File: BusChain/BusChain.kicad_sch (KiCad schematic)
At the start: 32 parts, among them J1 Bonn_01x07, J10 Bonn_01x04, J11 Bonn_01x04, J12 Bonn_01x04, J13 Bonn_01x04, J14 Bonn_01x04, J15 Bonn_01x04, J16 Bonn_01x04, J17 Bonn_01x04, J18 Bonn_01x07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

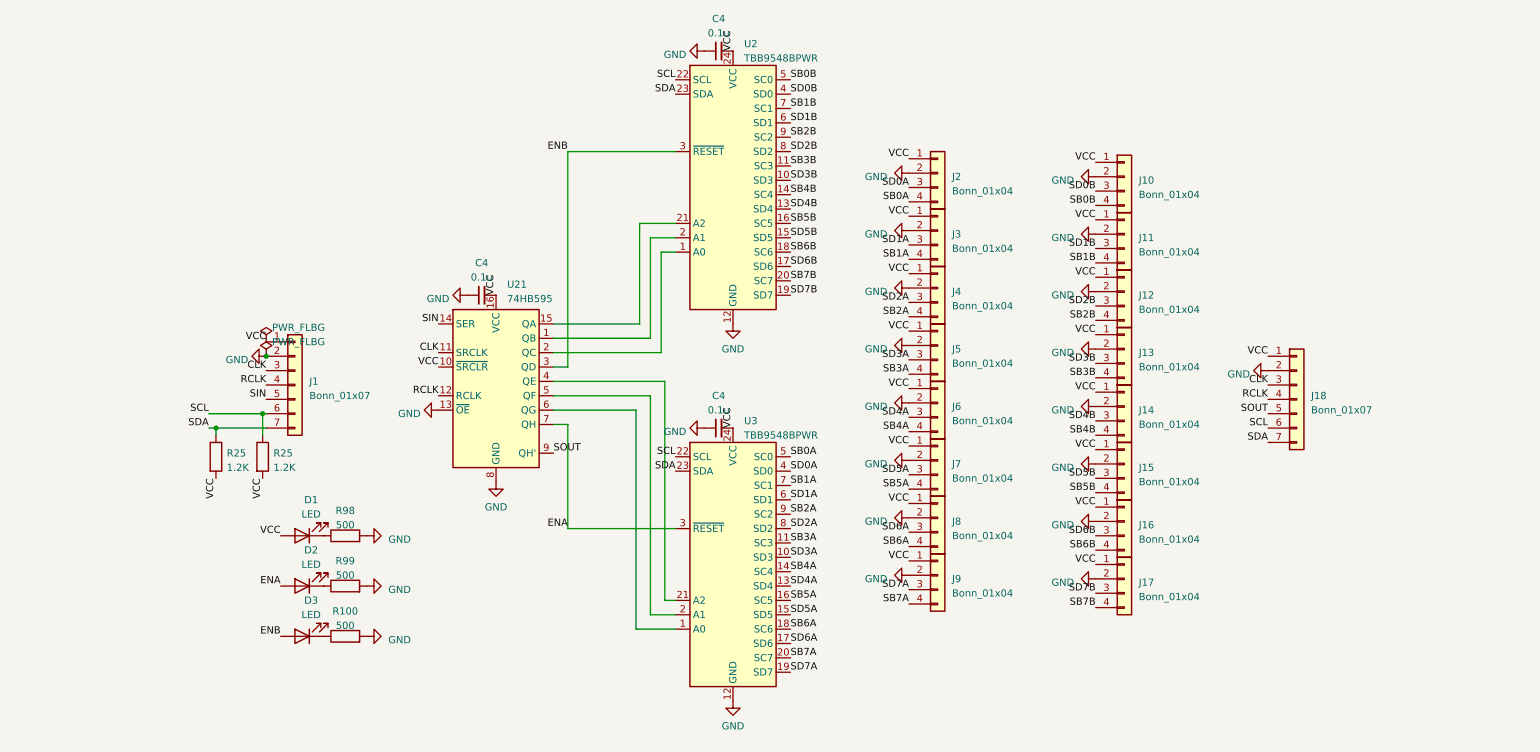
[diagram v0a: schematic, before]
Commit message: Finished BusChain PCB
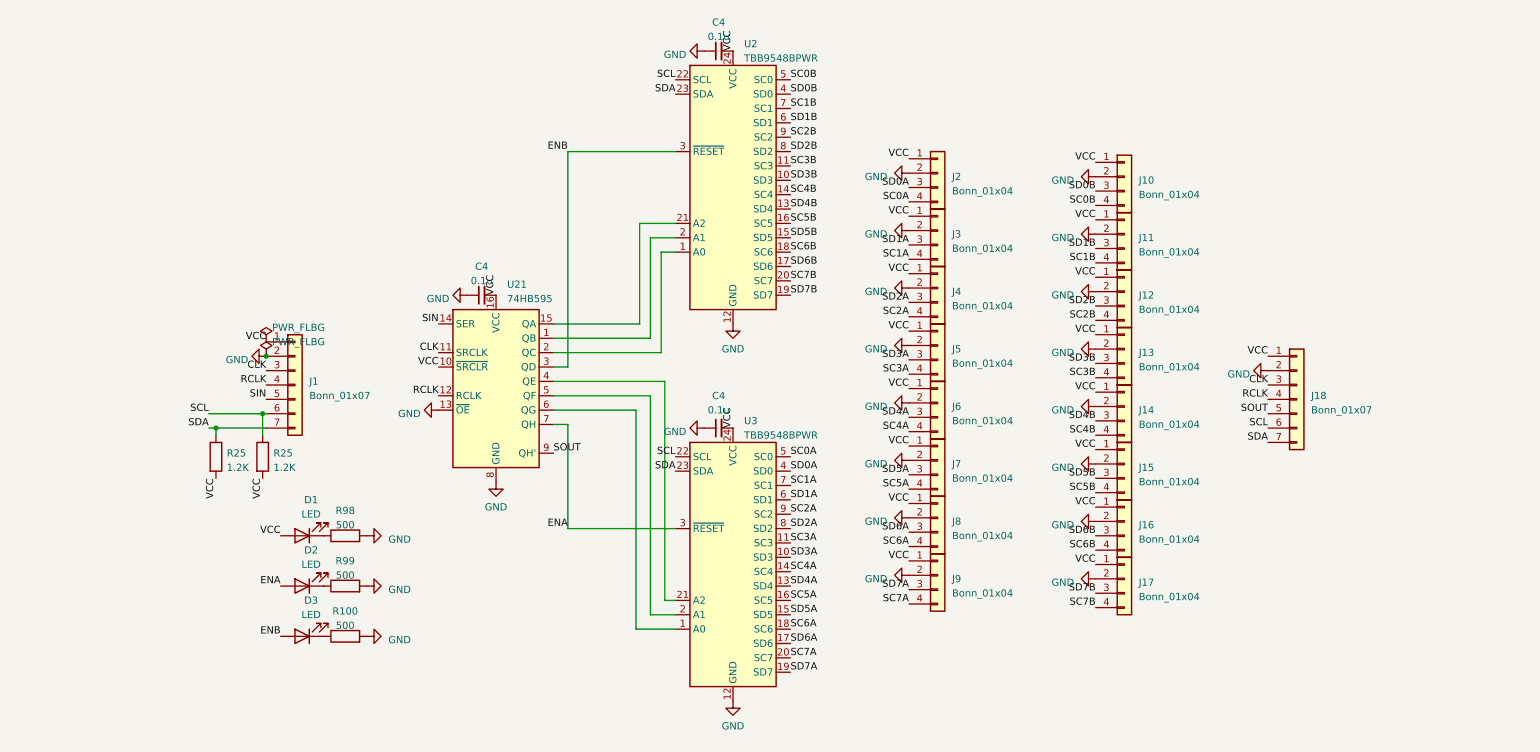
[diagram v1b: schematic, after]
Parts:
- J1: footprint Connector_PinHeader_2.54mm:PinHeader_1x07_P2.54mm_Vertical -> Connector_PinSocket_2.54mm:PinSocket_1x07_P2.54mm_Horizontal
- J18: footprint Connector_PinHeader_2.54mm:PinHeader_1x07_P2.54mm_Vertical -> Connector_PinHeader_2.54mm:PinHeader_1x07_P2.54mm_Horizontal
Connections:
- net SB0A renamed SC0A
- net SB0B renamed SC0B
- net SB1A renamed SC1A
- net SB1B renamed SC1B
- net SB2A renamed SC2A
- net SB2B renamed SC2B
- net SB3A renamed SC3A
- net SB3B renamed SC3B
- net SB4A renamed SC4A
- net SB4B renamed SC4B
- net SB5A renamed SC5A
- net SB5B renamed SC5B
- net SB6A renamed SC6A
- net SB6B renamed SC6B
- net SB7A renamed SC7A
- net SB7B renamed SC7B

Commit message: Finalized PCBs for fabrication
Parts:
- removed R25 (x2): 1.2K, Resistor_SMD:R_0402_1005Metric, symbol Device:R
- added C4 (x2): 0.1u, Capacitor_SMD:C_0402_1005Metric, symbol Device:C_Small
- added R98 (x2): 500, Resistor_SMD:R_0402_1005Metric, symbol Device:R
- added U2: MIC5365-3.3YC5, Package_TO_SOT_SMD:SOT-353_SC-70-5, symbol Regulator_Linear:MIC5365-3.3YC5
- renumbered U2 to U5, U3 to U6
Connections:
- net GND: now also C4.2, C4.2, U2.2 (GND)
- net SCL: now also R98.2
- net SDA: now also R98.2
- net VCC: now also C4.1, R98.1, R98.1, U2.5 (VOUT); no longer J1.1 (Pin_1)
- new net V?: C4.1, J1.1 (Pin_1), U2.1 (VIN)
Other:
- moved on the sheet: C4, D1, D2, D3, J1, J10, J11, J12, J13, J14, J15, J16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

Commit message: Resolved various production and testing issues
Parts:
- J1, J18: value Bonn_01x07 -> Conn_01x07
- J10, J11, J12, J13, J14, J15, J16, J17, J2, J3, J4, J5, J6, J7, J8, J9: value Bonn_01x04 -> Conn_01x04
- R98: value 500 -> 1.2K
- U21: value 74HB595 -> 74HC595
- U5, U6: value TBB9548BPWR -> TCA9548BPWR
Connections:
- net V?: now also U2.3 (EN)
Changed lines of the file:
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@@
   (junction (at 55.88 55.88) (diameter 0) (color 0 0 0 0)
   )
+  (junction (at 60.325 55.88) (diameter 0) (color 0 0 0 0)
+  )
   (wire (pts (xy 137.795 97.79) (xy 135.255 97.79))
     (stroke (width 0) (type default))
@@
   )
   (wire (pts (xy 152.4 64.77) (xy 156.845 64.77))
+    (stroke (width 0) (type default))
+  )
+  (wire (pts (xy 60.325 55.88) (xy 60.325 60.96))
     (stroke (width 0) (type default))
   )
@@
       (effects (font (size 1.27 1.27)) (justify left))
     )
-    (property "Value" "Bonn_01x04" (at 238.76 67.31 0)
+    (property "Value" "Conn_01x04" (at 238.76 67.31 0)
       (effects (font (size 1.27 1.27)) (justify left))
     )
@@
       (effects (font (size 1.27 1.27)) (justify left))
     )
-    (property "Value" "Bonn_01x04" (at 205.74 107.315 0)
+    (property "Value" "Conn_01x04" (at 205.74 107.315 0)
       (effects (font (size 1.27 1.27)) (justify left))
     )
@@
       (effects (font (size 1.27 1.27)) (justify right))
     )
-    (property "Value" "500" (at 26.67 76.835 0)
+    (property "Value" "1.2K" (at 26.67 76.835 0)
       (effects (font (size 1.27 1.27)) (justify right))
     )
@@
       (effects (font (size 1.27 1.27)) (justify left))
     )
-    (property "Value" "Bonn_01x04" (at 238.76 87.63 0)
+    (property "Value" "Conn_01x04" (at 238.76 87.63 0)
       (effects (font (size 1.27 1.27)) (justify left))
     )
@@
       (effects (font (size 1.27 1.27)) (justify left))
     )
-    (property "Value" "Bonn_01x04" (at 205.74 117.475 0)
+    (property "Value" "Conn_01x04" (at 205.74 117.475 0)
       (effects (font (size 1.27 1.27)) (justify left))
     )
@@
       (effects (font (size 1.27 1.27)) (justify left))
     )
-    (property "Value" "Bonn_01x07" (at 269.24 95.25 0)
+    (property "Value" "Conn_01x07" (at 269.24 95.25 0)
       (effects (font (size 1.27 1.27)) (justify left))
     )
@@
       (effects (font (size 1.27 1.27)) (justify left))
     )
-    (property "Value" "Bonn_01x04" (at 205.74 76.835 0)
+    (property "Value" "Conn_01x04" (at 205.74 76.835 0)
       (effects (font (size 1.27 1.27)) (justify left))
     )
@@
       (effects (font (size 1.27 1.27)) (justify left))
     )
-    (property "Value" "Bonn_01x04" (at 238.76 107.95 0)
+    (property "Value" "Conn_01x04" (at 238.76 107.95 0)
       (effects (font (size 1.27 1.27)) (justify left))
     )
@@
       (effects (font (size 1.27 1.27)) (justify left))
     )
-    (property "Value" "Bonn_01x04" (at 238.76 128.27 0)
+    (property "Value" "Conn_01x04" (at 238.76 128.27 0)
       (effects (font (size 1.27 1.27)) (justify left))
     )
@@
       (effects (font (size 1.27 1.27)) (justify left))
     )
-    (property "Value" "Bonn_01x04" (at 205.74 66.675 0)
+    (property "Value" "Conn_01x04" (at 205.74 66.675 0)
       (effects (font (size 1.27 1.27)) (justify left))
     )
@@
       (effects (font (size 1.27 1.27)) (justify left))
     )
-    (property "Value" "Bonn_01x07" (at 41.275 64.135 0)
+    (property "Value" "Conn_01x07" (at 41.275 64.135 0)
       (effects (font (size 1.27 1.27)) (justify left))
     )
@@
       (effects (font (size 1.27 1.27)) (justify left))
     )
-    (property "Value" "TBB9548BPWR" (at 168.9609 33.02 0)
+    (property "Value" "TCA9548BPWR" (at 168.9609 33.02 0)
       (effects (font (size 1.27 1.27)) (justify left))
     )
@@
       (effects (font (size 1.27 1.27)) (justify left))
     )
-    (property "Value" "Bonn_01x04" (at 205.74 86.995 0)
+    (property "Value" "Conn_01x04" (at 205.74 86.995 0)
       (effects (font (size 1.27 1.27)) (justify left))
     )
@@
       (effects (font (size 1.27 1.27)) (justify left))
     )
-    (property "Value" "Bonn_01x04" (at 205.74 127.635 0)
+    (property "Value" "Conn_01x04" (at 205.74 127.635 0)
       (effects (font (size 1.27 1.27)) (justify left))
     )
@@
       (effects (font (size 1.27 1.27)) (justify left))
     )
-    (property "Value" "Bonn_01x04" (at 238.76 118.11 0)
+    (property "Value" "Conn_01x04" (at 238.76 118.11 0)
       (effects (font (size 1.27 1.27)) (justify left))
     )
@@
       (effects (font (size 1.27 1.27)) (justify left))
     )
-    (property "Value" "Bonn_01x04" (at 238.76 77.47 0)
+    (property "Value" "Conn_01x04" (at 238.76 77.47 0)
       (effects (font (size 1.27 1.27)) (justify left))
     )
@@
       (effects (font (size 1.27 1.27)) (justify left))
     )
-    (property "Value" "Bonn_01x04" (at 238.76 97.79 0)
+    (property "Value" "Conn_01x04" (at 238.76 97.79 0)
       (effects (font (size 1.27 1.27)) (justify left))
     )
@@
       (effects (font (size 1.27 1.27)) (justify left))
     )
-    (property "Value" "Bonn_01x04" (at 205.74 97.155 0)
+    (property "Value" "Conn_01x04" (at 205.74 97.155 0)
       (effects (font (size 1.27 1.27)) (justify left))
     )
@@
       (effects (font (size 1.27 1.27)) (justify left))
     )
-    (property "Value" "Bonn_01x04" (at 205.74 56.515 0)
+    (property "Value" "Conn_01x04" (at 205.74 56.515 0)
       (effects (font (size 1.27 1.27)) (justify left))
     )
@@
       (effects (font (size 1.27 1.27)) (justify left))
     )
-    (property "Value" "Bonn_01x04" (at 238.76 57.15 0)
+    (property "Value" "Conn_01x04" (at 238.76 57.15 0)
       (effects (font (size 1.27 1.27)) (justify left))
     )
@@
   (symbol (lib_id "74xx:74HC595") (at 125.095 90.17 0) (unit 1)
     (in_bom yes) (on_board yes) (dnp no) (fields_autoplaced)
-    (property "Reference" "U21" (at 127.0509 73.025 0)
-      (effects (font (size 1.27 1.27)) (justify left))
-    )
-    (property "Value" "74HB595" (at 127.0509 75.565 0)
+    (property "Reference" "U21" (at 127.0509 73.66 0)
+      (effects (font (size 1.27 1.27)) (justify left))
+    )
+    (property "Value" "74HC595" (at 127.0509 76.2 0)
       (effects (font (size 1.27 1.27)) (justify left))
     )
@@
   (symbol (lib_id "Interface_Expansion:TCA9548APWR") (at 167.005 121.285 0) (unit 1)
     (in_bom yes) (on_board yes) (dnp no) (fields_autoplaced)
-    (property "Reference" "U6" (at 168.9609 97.155 0)
-      (effects (font (size 1.27 1.27)) (justify left))
-    )
-    (property "Value" "TBB9548BPWR" (at 168.9609 99.695 0)
+    (property "Reference" "U6" (at 168.9609 96.52 0)
+      (effects (font (size 1.27 1.27)) (justify left))
+    )
+    (property "Value" "TCA9548BPWR" (at 168.9609 99.06 0)
       (effects (font (size 1.27 1.27)) (justify left))
     )
@@
       (effects (font (size 1.27 1.27)) (justify right))
     )
-    (property "Value" "500" (at 34.29 76.835 0)
+    (property "Value" "1.2K" (at 34.29 76.835 0)
       (effects (font (size 1.27 1.27)) (justify right))
     )
@@
   )
   (symbol (lib_id "Device:C_Small") (at 55.88 58.42 0) (unit 1)
-    (in_bom yes) (on_board yes) (dnp no) (fields_autoplaced)
+    (in_bom yes) (on_board yes) (dnp no)
     (property "Reference" "C4" (at 58.42 57.7913 0)
       (effects (font (size 1.27 1.27)) (justify left))
     )
-    (property "Value" "0.1u" (at 58.42 60.3313 0)
-      (effects (font (size 1.27 1.27)) (justify left))
-    )
+    (property "Value" "0.1u" (at 58.42 58.42 0)
+      (effects (font (size 1.27 1.27)) (justify left))
+    )

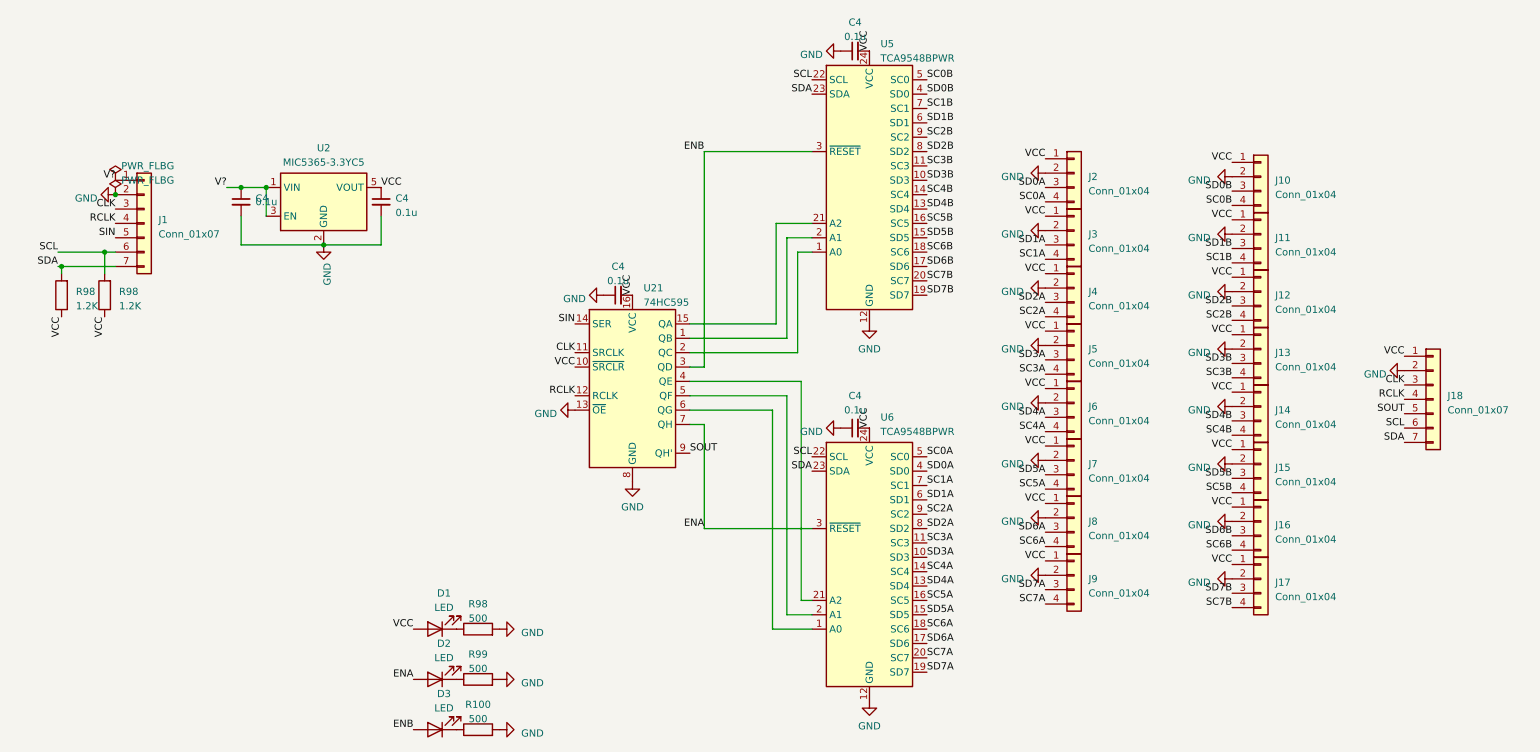
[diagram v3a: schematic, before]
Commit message: Finished BusChain1.1 and added power daisy-chaining option
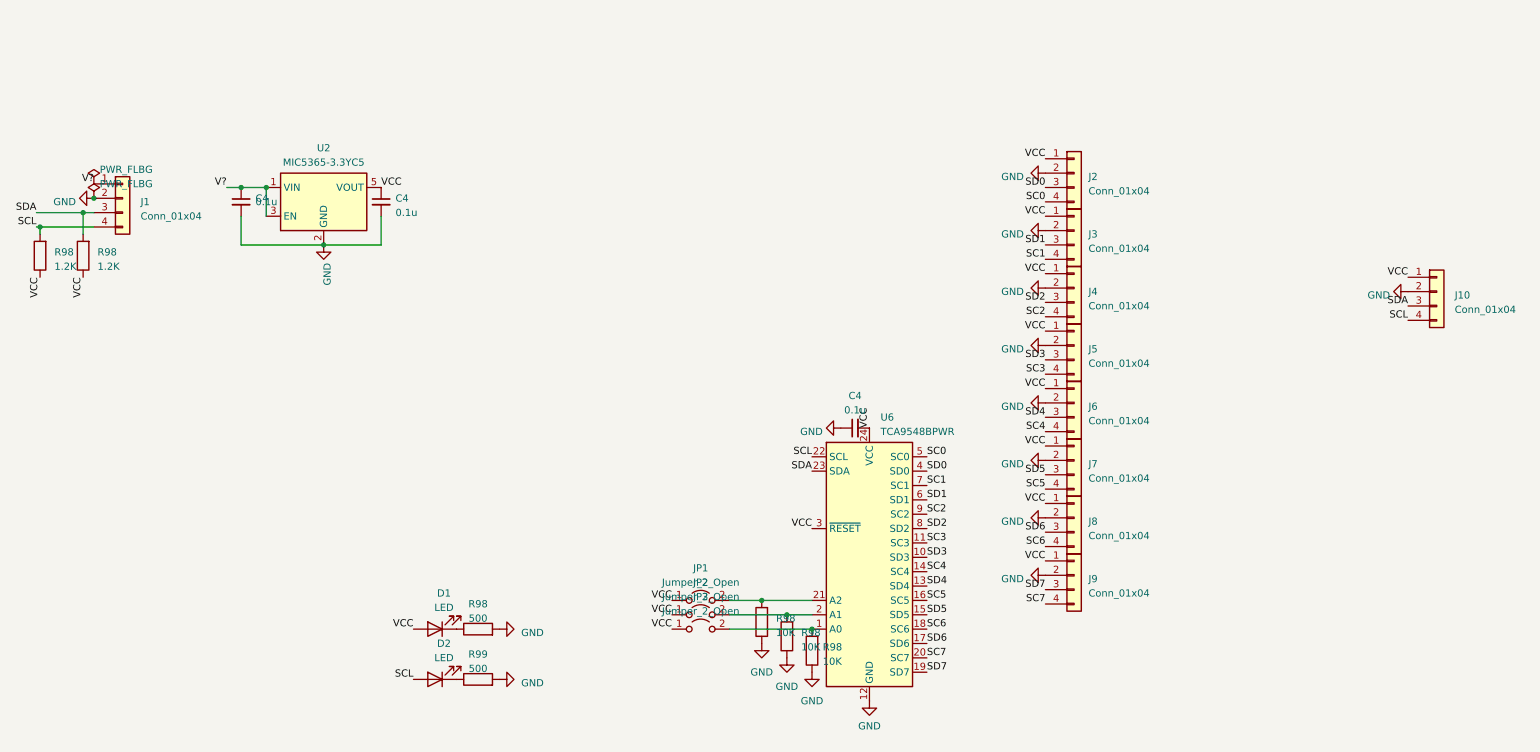
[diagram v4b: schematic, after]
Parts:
- removed C4 (x2): 0.1u, Capacitor_SMD:C_0402_1005Metric, symbol Device:C_Small
- removed D3: LED, LED_SMD:LED_0603_1608Metric, symbol Device:LED
- removed J1: Conn_01x07, Connector_PinSocket_2.54mm:PinSocket_1x07_P2.54mm_Horizontal, symbol Connector_Generic:Conn_01x07
- removed J11, J12, J13, J14, J15, J16, J17: Conn_01x04, Connector_PinHeader_2.54mm:PinHeader_1x04_P2.54mm_Vertical, symbol Connector_Generic:Conn_01x04
- removed J18: Conn_01x07, Connector_PinHeader_2.54mm:PinHeader_1x07_P2.54mm_Horizontal, symbol Connector_Generic:Conn_01x07
- removed R100: 500, Resistor_SMD:R_0402_1005Metric, symbol Device:R
- removed U21: 74HC595, Package_SO:TSSOP-16_4.4x5mm_P0.65mm, symbol 74xx:74HC595
- removed U5: TCA9548BPWR, Package_SO:TSSOP-24_4.4x7.8mm_P0.65mm, symbol Interface_Expansion:TCA9548APWR
- added J1: Conn_01x04, Connector_PinSocket_2.54mm:PinSocket_1x04_P2.54mm_Horizontal, symbol Connector_Generic:Conn_01x04
- added JP1, JP2, JP3: Jumper_2_Open, Jumper:SolderJumper-2_P1.3mm_Open_RoundedPad1.0x1.5mm, symbol Jumper:Jumper_2_Open
- added R98 (x3): 10K, Resistor_SMD:R_0402_1005Metric, symbol Device:R
- J10: footprint Connector_PinHeader_2.54mm:PinHeader_1x04_P2.54mm_Vertical -> Connector_PinHeader_2.54mm:PinHeader_1x04_P2.54mm_Horizontal
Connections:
- net SC0B is gone; now on net SCL: J10.4 (Pin_4)
- net SD0B is gone; now on net SDA: J10.3 (Pin_3)
- net GND: now also J1.2 (Pin_2), R98.1, R98.1, R98.1
- net SCL: now also D2.2 (A), R98.2, J1.4 (Pin_4); no longer R98.2
- net SDA: now also R98.2, J1.3 (Pin_3); no longer R98.2
- net V?: now also J1.1 (Pin_1)
- net VCC: now also U6.3 (~{RESET}), JP1.1 (A), JP2.1 (A), JP3.1 (A)
- net at U6.21 (A2): now also JP1.2 (B), R98.2
- net at U6.2 (A1): now also JP2.2 (B), R98.2
- net at U6.1 (A0): now also JP3.2 (B), R98.2
- removed net ENA: D2.2 (A), U6.3 (~{RESET})
- net SC0A renamed SC0
- net SC1A renamed SC1
- net SC2A renamed SC2
- net SC3A renamed SC3
- net SC4A renamed SC4
- net SC5A renamed SC5
- net SC6A renamed SC6
- net SC7A renamed SC7
- net SD0A renamed SD0
- net SD1A renamed SD1
- net SD2A renamed SD2
- net SD3A renamed SD3
- net SD4A renamed SD4
- net SD5A renamed SD5
- net SD6A renamed SD6
- net SD7A renamed SD7
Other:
- moved on the sheet: R98
